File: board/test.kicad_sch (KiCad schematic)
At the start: 2 parts, among them SW1 RotaryEncoder_Switch

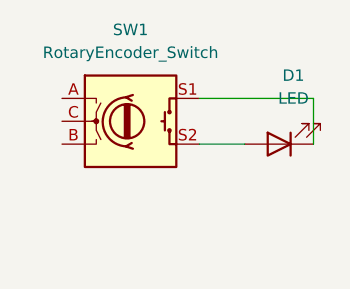
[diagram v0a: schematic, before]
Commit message: removed 2 wires in test.kicad_sch
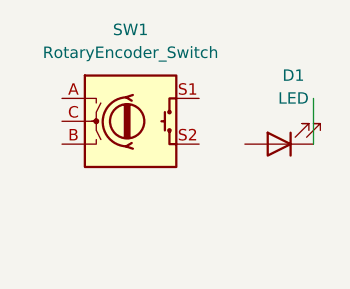
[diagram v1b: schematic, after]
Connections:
- net at SW1.S1: no longer D1.1 (K)
- net at SW1.S2: no longer D1.2 (A)
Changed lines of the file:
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@@
-	(wire
-		(pts
-			(xy 100.33 101.6) (xy 113.03 101.6)
-		)
-		(stroke
-			(width 0)
-			(type default)
-		)
-	)
-	(wire
-		(pts
-			(xy 100.33 106.68) (xy 105.41 106.68)
-		)
-		(stroke
-			(width 0)
-			(type default)
-		)
-	)
 	(wire
 		(pts

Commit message: added 3 wires, modified 1 wire in test.kicad_sch
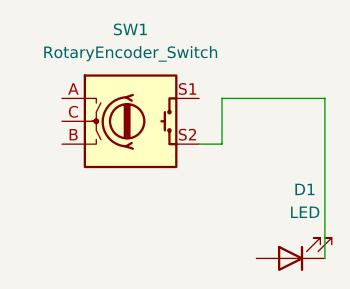
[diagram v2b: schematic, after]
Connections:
- net at SW1.S2: now also D1.1 (K)
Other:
- moved on the sheet: D1
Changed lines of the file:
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@@
 	(wire
 		(pts
-			(xy 113.03 101.6) (xy 113.03 106.68)
+			(xy 114.3 101.6) (xy 102.87 101.6)
+		)
+		(stroke
+			(width 0)
+			(type default)
+		)
+	)
+	(wire
+		(pts
+			(xy 102.87 101.6) (xy 102.87 106.68)
+		)
+		(stroke
+			(width 0)
+			(type default)
+		)
+	)
+	(wire
+		(pts
+			(xy 102.87 106.68) (xy 100.33 106.68)
+		)
+		(stroke
+			(width 0)
+			(type default)
+		)
+	)
+	(wire
+		(pts
+			(xy 114.3 101.6) (xy 114.3 119.38)
 		)
 		(stroke
@@
 	(symbol
 		(lib_id "Device:LED")
-		(at 109.22 106.68 180)
+		(at 110.49 119.38 180)
 		(unit 1)
 		(exclude_from_sim no)
@@
 		(fields_autoplaced yes)
 		(property "Reference" "D1"
-			(at 110.8075 99.06 0)
+			(at 112.0775 111.76 0)
 			(effects
 				(font
@@
 		)
 		(property "Value" "LED"
-			(at 110.8075 101.6 0)
+			(at 112.0775 114.3 0)
 			(effects
 				(font
@@
 		)
 		(property "Footprint" ""
-			(at 109.22 106.68 0)
+			(at 110.49 119.38 0)
 			(effects
 				(font
@@
 		)
 		(property "Datasheet" "~"
-			(at 109.22 106.68 0)
+			(at 110.49 119.38 0)
 			(effects
 				(font
@@
 		)
 		(property "Description" "Light emitting diode"
-			(at 109.22 106.68 0)
+			(at 110.49 119.38 0)
 			(effects
 				(font
@@
 		)
 		(property "Sim.Pins" "1=K 2=A"
-			(at 109.22 106.68 0)
+			(at 110.49 119.38 0)
 			(effects
 				(font
